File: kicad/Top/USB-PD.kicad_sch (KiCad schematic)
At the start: 46 parts, among them U3 MCP1804 SOT-23-5

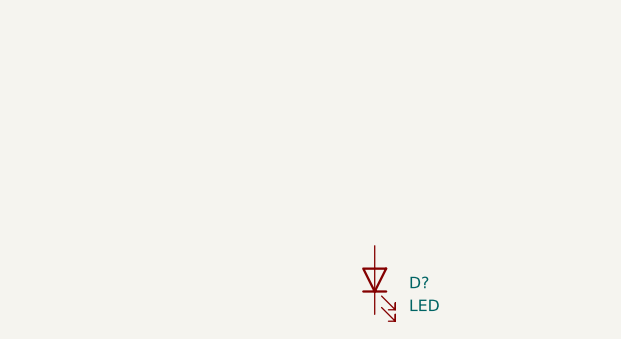
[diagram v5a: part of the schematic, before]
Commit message: Removed random LED floating in sch
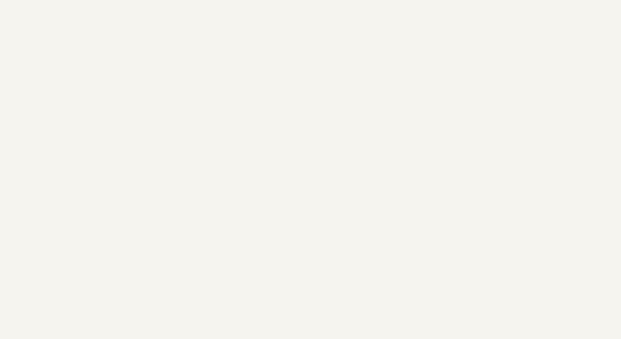
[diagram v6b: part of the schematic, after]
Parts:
- removed D?: LED, symbol Device:LED
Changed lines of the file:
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@@
-    (pin "2")
-  )
-  (symbol (lib_id "Device:LED") (at 715.01 525.78 90) (unit 1)
-    (in_bom yes) (on_board yes) (fields_autoplaced)
-    (property "Reference" "D?" (id 0) (at 718.82 526.0974 90)
-      (effects (font (size 1.27 1.27)) (justify right))
-    )
-    (property "Value" "LED" (id 1) (at 718.82 528.6374 90)
-      (effects (font (size 1.27 1.27)) (justify right))
-    )
-    (property "Footprint" "" (id 2) (at 715.01 525.78 0)
-      (effects (font (size 1.27 1.27)) hide)
-    )
-    (property "Datasheet" "~" (id 3) (at 715.01 525.78 0)
-      (effects (font (size 1.27 1.27)) hide)
-    )
-    (pin "1")
     (pin "2")
   )

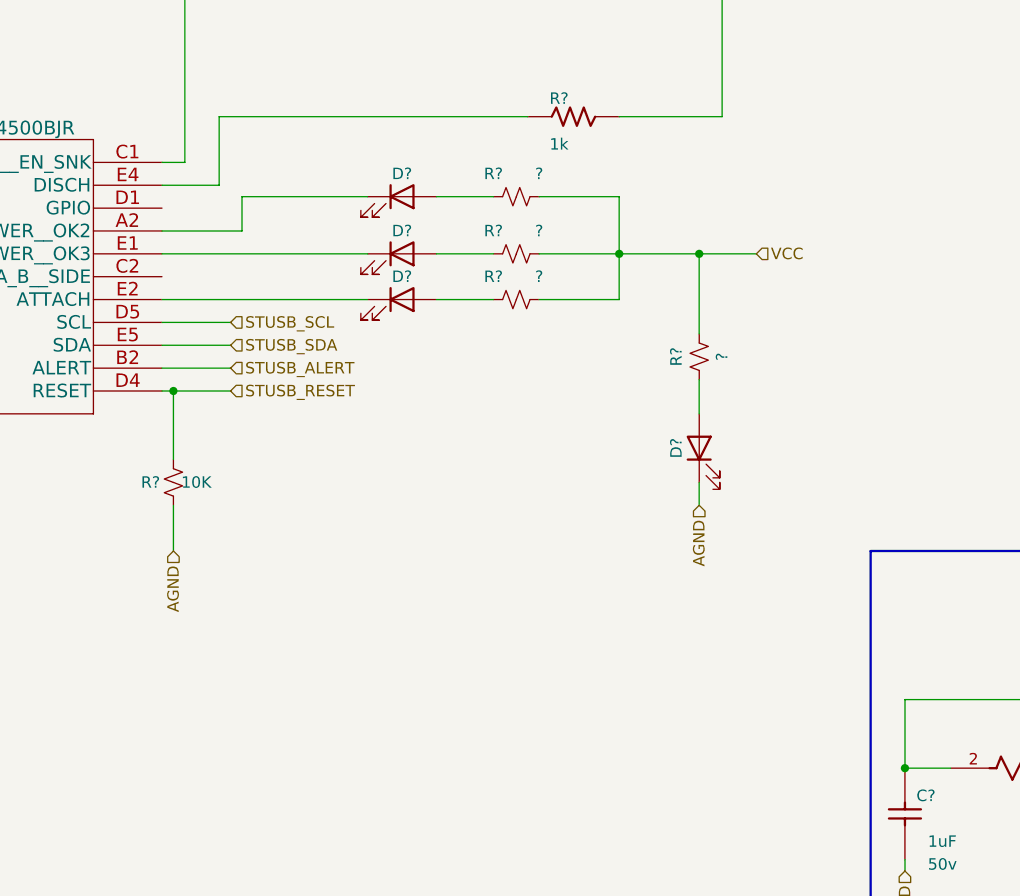
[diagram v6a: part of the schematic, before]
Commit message: Added pull up resistors to mcu comm ports
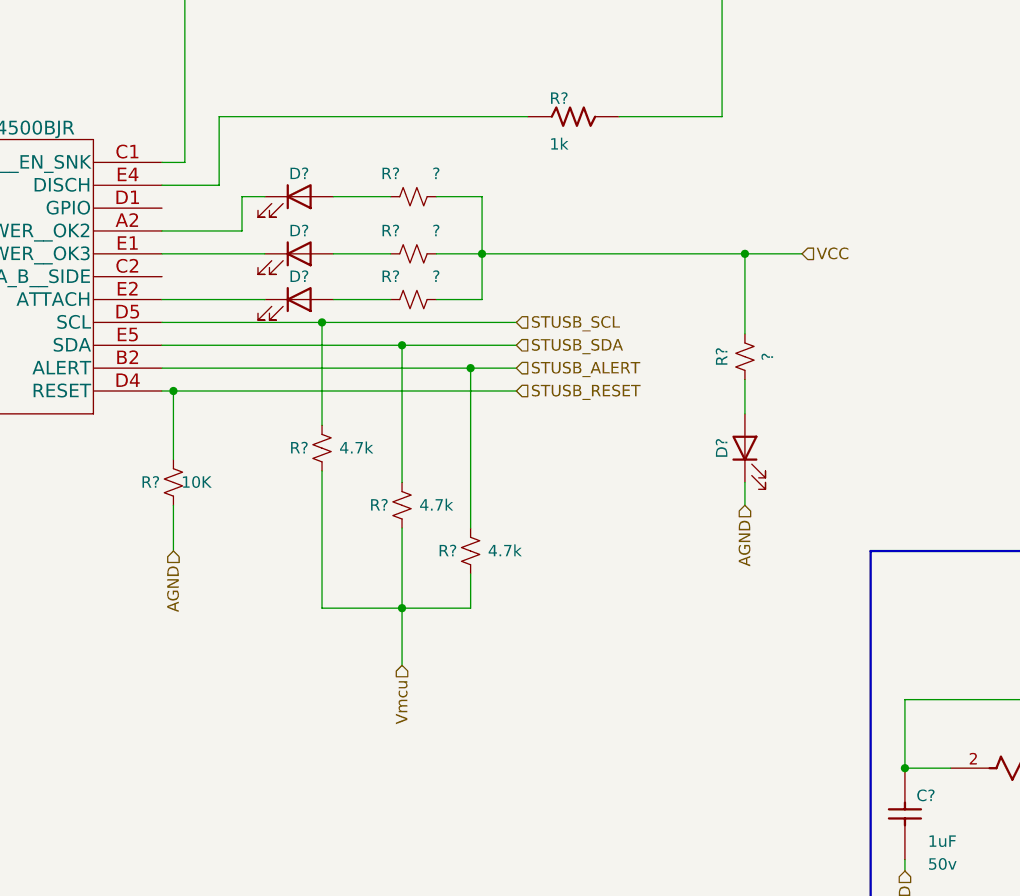
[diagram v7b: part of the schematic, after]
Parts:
- added R? (x3): 4.7k, symbol Device:R_Small_US
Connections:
- net STUSB_ALERT: now also R?.2
- net STUSB_SCL: now also R?.2
- net STUSB_SDA: now also R?.2
- new net Vmcu: R?.1, R?.1, R?.1
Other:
- moved on the sheet: D?, R?

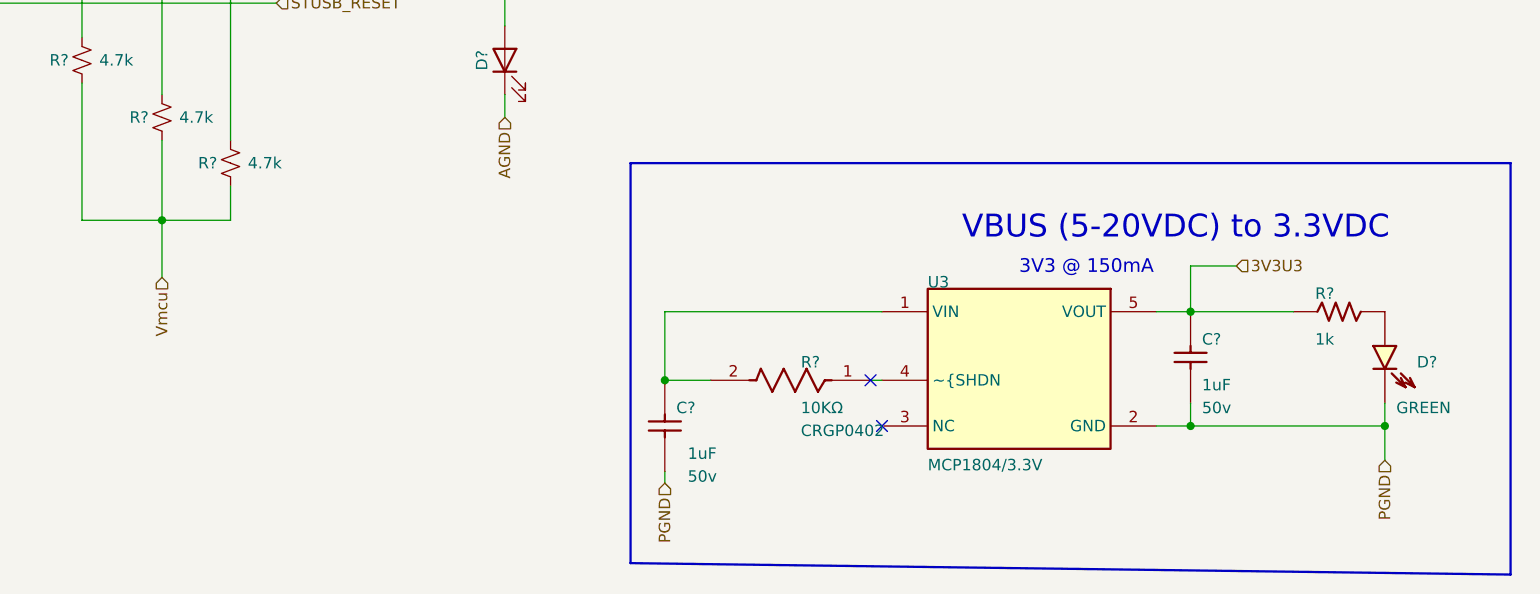
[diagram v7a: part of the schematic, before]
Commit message: Merged LDOs and moved to top sheet
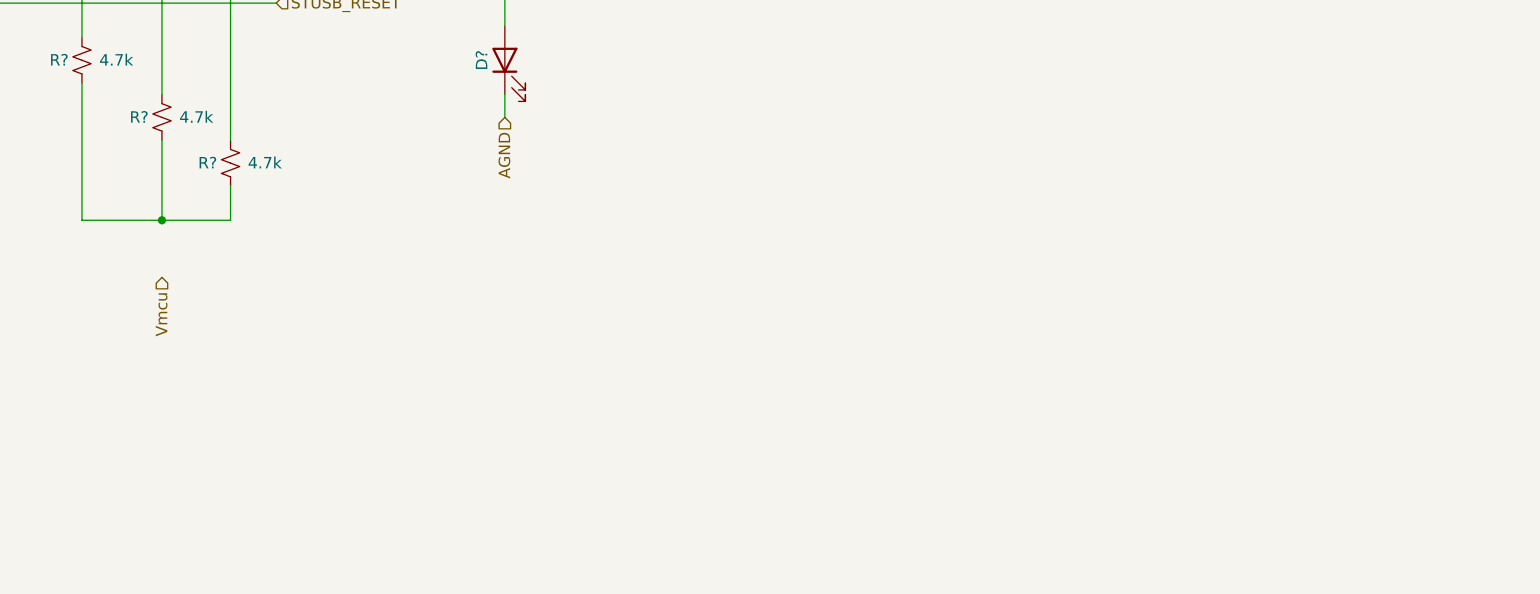
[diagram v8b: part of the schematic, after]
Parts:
- removed C? (x2): Capacitor NP, AltiumImports:_ALTIUM_WORK_00001_MCHP-CDB_Library_Database_.._Footprints_CAP_C_0603.PcbLib_CAP_C_0603, symbol Top-altium-import:1_Capacitor NP
- removed D?: LED_green, AltiumImports:_ALTIUM_WORK_00001_MCHP-CDB_Library_Database_.._Footprints_LED_0603_Green.PcbLib_LED_0603_GREEN, symbol Top-altium-import:3_LED_green
- removed R?: CRGP0402F10K, AltiumImports:FP-CRGP0402-IPC_A, symbol Top-altium-import:2_CMP-03211-008310-1
- removed R?: Resistor, AltiumImports:_ALTIUM_WORK_00001_MCHP-CDB_Library_Database_MCHP-CDB.DbLib_Resistor_RES_C_0402, symbol Top-altium-import:2_Resistor
- removed U3: MCP1804 SOT-23-5, AltiumImports:_ALTIUM_WORK_00001_MCHP-CDB_Library_Database_MCHP-CDB.DbLib_MCHP-Analog_SOT-23-5, symbol Top-altium-import:0_MCP1804 SOT-23-5
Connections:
- net Vmcu: no longer R?.1, R?.1, R?.1
- new net: R?.1, R?.1, R?.1
- no-connect marks 12 -> 10
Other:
- note removed: "3V3 @ 150mA"
- note removed: "VBUS (5-20VDC) to 3.3VDC"
